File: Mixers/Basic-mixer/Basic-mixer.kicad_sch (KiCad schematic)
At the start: 37 parts, among them J1 In, J2 Power Input, J3 In, J4 Out, J5 In, J6 In, SW1 Mute, SW2 Mute, SW3 Mute, SW4 Mute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

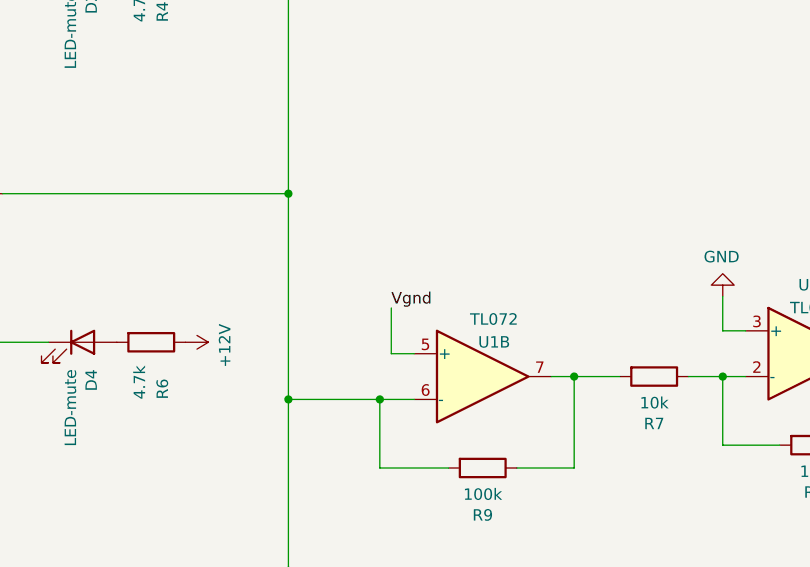
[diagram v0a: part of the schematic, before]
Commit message: Fix GND link to inv Opamp 1
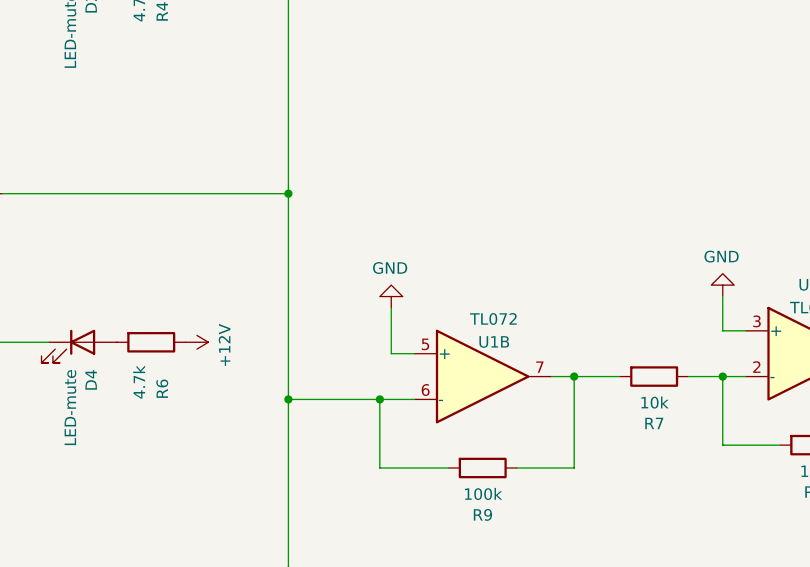
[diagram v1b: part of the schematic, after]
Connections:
- net Vgnd is gone; now on net GND: U1.5 (+)
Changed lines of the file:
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@@
-    (effects (font (size 1.27 1.27)) (justify left bottom))
-  )
-  (label "Vgnd" (at 120.65 105.41 0)
     (effects (font (size 1.27 1.27)) (justify left bottom))
   )
@@
     (pin "TN")
   )
+  (symbol (lib_id "power:GND") (at 120.65 105.41 180) (unit 1)
+    (in_bom yes) (on_board yes)
+    (property "Reference" "#PWR?" (id 0) (at 120.65 99.06 0)
+      (effects (font (size 1.27 1.27)) hide)
+    )
+    (property "Value" "GND" (id 1) (at 120.523 101.0158 0))
+    (property "Footprint" "" (id 2) (at 120.65 105.41 0)
+      (effects (font (size 1.27 1.27)) hide)
+    )
+    (property "Datasheet" "" (id 3) (at 120.65 105.41 0)
+      (effects (font (size 1.27 1.27)) hide)
+    )
+    (pin "1")
+  )
   (symbol (lib_id "Switch:SW_Push_DPDT") (at 58.42 76.2 270) (unit 1)
     (in_bom yes) (on_board yes)
@@
       (reference "#PWR026") (unit 1) (value "GND") (footprint "")
     )
+    (path "/20610dee-24a2-4a35-9d47-947d8d2d938e"
+      (reference "#PWR?") (unit 1) (value "GND") (footprint "")
+    )
     (path "/5a024088-6937-4126-bed0-b3d42ebf7a88"
